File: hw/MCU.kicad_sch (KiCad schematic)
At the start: 19 parts, among them J2 Conn_01x06, J7 Conn_01x04, SW2 SKRPACE010, SW3 SKRPACE010, U2 N32L406RBL7, Y2 XL2EL89COI-111YLC-8M

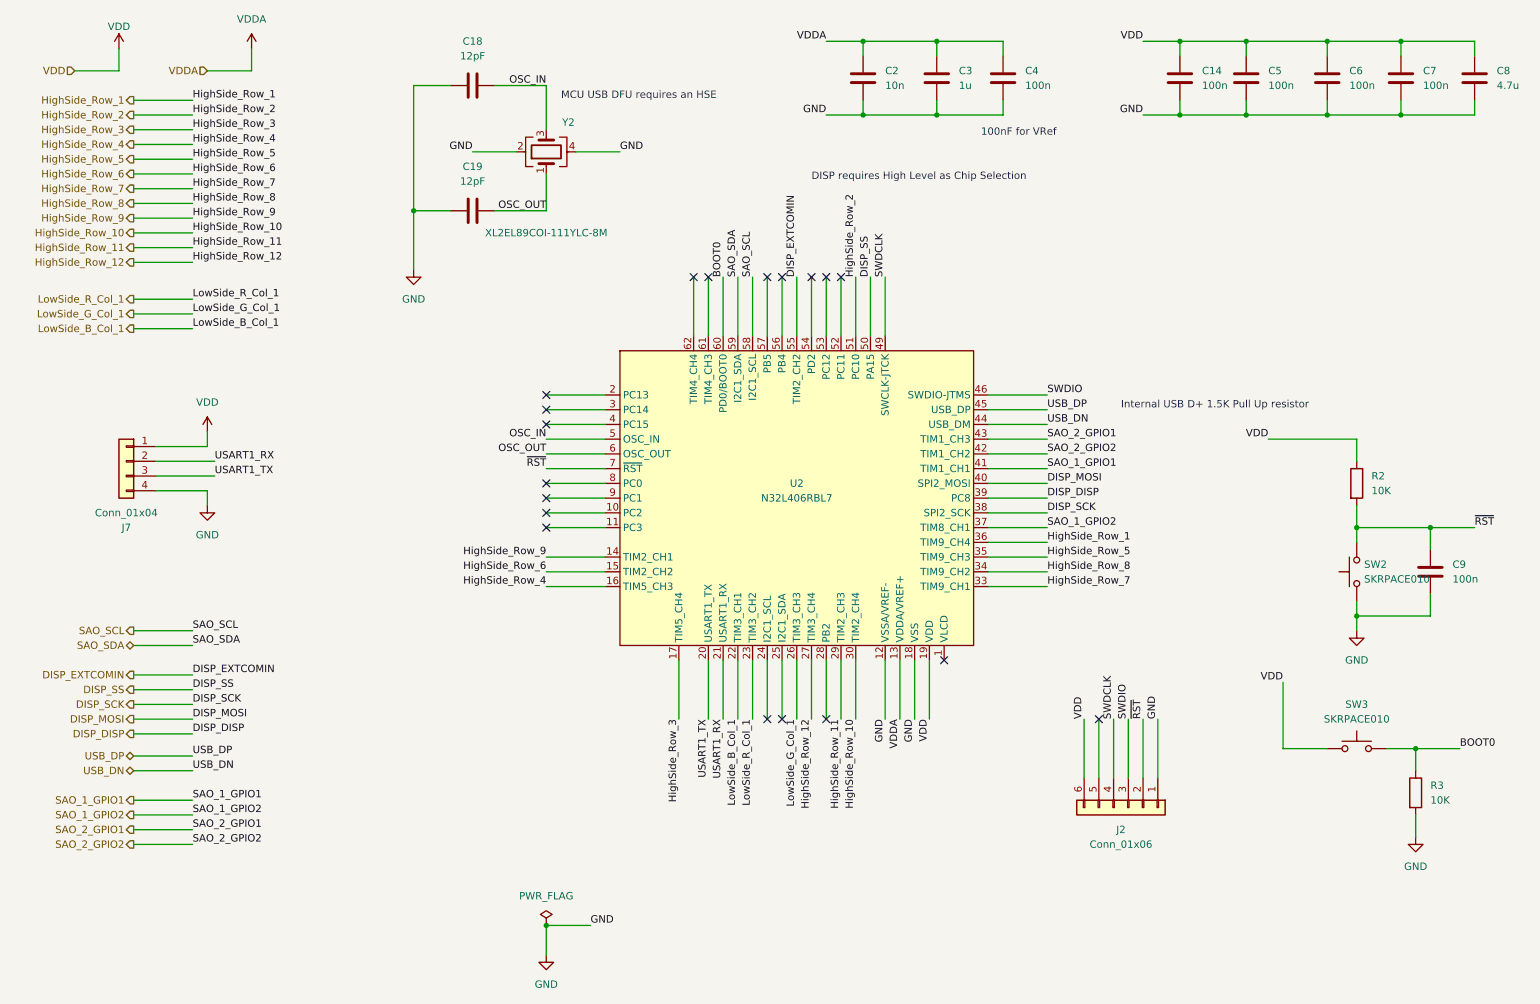
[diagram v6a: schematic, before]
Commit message: changed some pin connections
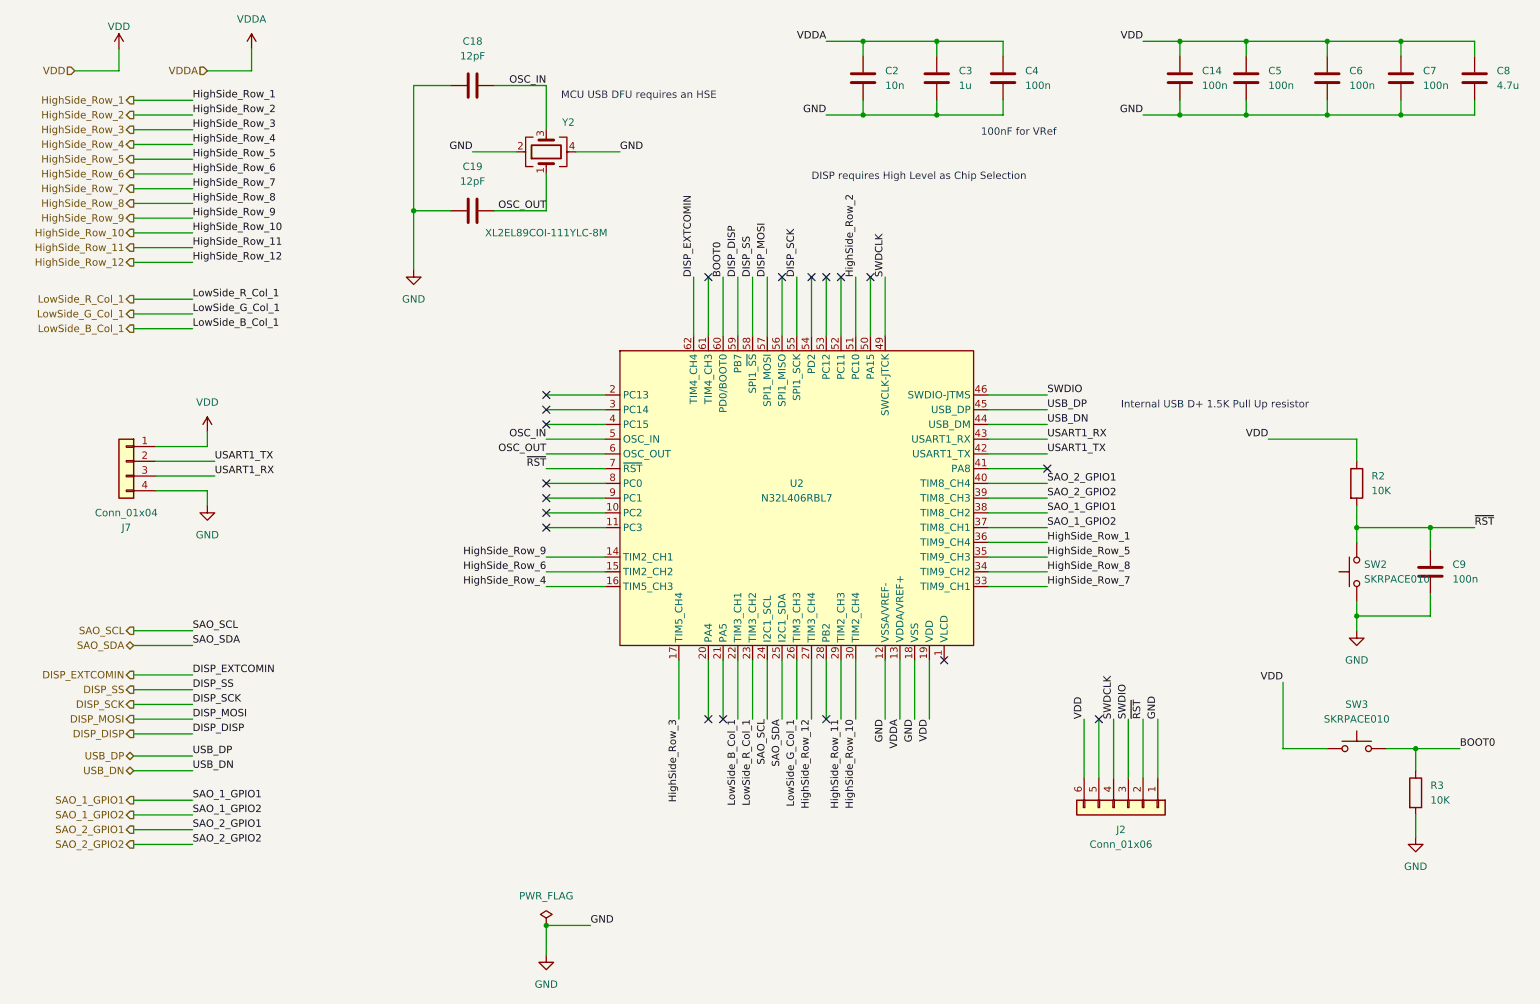
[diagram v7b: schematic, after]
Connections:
- net DISP_DISP: now also U2.59 (PB7); no longer U2.39 (PC8)
- net DISP_EXTCOMIN: now also U2.62 (PB9); no longer U2.55 (PB3)
- net DISP_MOSI: now also U2.57 (PB5); no longer U2.40 (PC9)
- net DISP_SCK: now also U2.55 (PB3); no longer U2.38 (PC7)
- net DISP_SS: now also U2.58 (PB6); no longer U2.50 (PA15)
- net SAO_1_GPIO1: now also U2.38 (PC7); no longer U2.41 (PA8)
- net SAO_2_GPIO1: now also U2.40 (PC9); no longer U2.43 (PA10)
- net SAO_2_GPIO2: now also U2.39 (PC8); no longer U2.42 (PA9)
- net SAO_SCL: now also U2.24 (PC4); no longer U2.58 (PB6)
- net SAO_SDA: now also U2.25 (PC5); no longer U2.59 (PB7)
- net USART1_RX: now also J7.3 (Pin_3), U2.43 (PA10); no longer J7.2 (Pin_2), U2.21 (PA5)
- net USART1_TX: now also J7.2 (Pin_2), U2.42 (PA9); no longer J7.3 (Pin_3), U2.20 (PA4)
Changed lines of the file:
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@@
   (no_connect (at 182.88 127))
   (no_connect (at 162.56 60.96))
-  (no_connect (at 154.94 137.16))
-  (no_connect (at 152.4 137.16))
   (no_connect (at 142.24 60.96))
+  (no_connect (at 170.18 60.96))
+  (no_connect (at 142.24 137.16))
+  (no_connect (at 200.66 93.98))
   (no_connect (at 114.3 86.36))
-  (no_connect (at 139.7 60.96))
+  (no_connect (at 154.94 60.96))
   (no_connect (at 114.3 99.06))
   (no_connect (at 209.55 137.16))
   (no_connect (at 114.3 96.52))
   (no_connect (at 165.1 60.96))
-  (no_connect (at 152.4 60.96))
   (no_connect (at 160.02 60.96))
   (no_connect (at 114.3 81.28))
-  (no_connect (at 154.94 60.96))
+  (no_connect (at 144.78 137.16))
   (no_connect (at 114.3 104.14))
   (no_connect (at 114.3 83.82))
@@
     (effects (font (size 1.27 1.27)) (justify right bottom))
   )
-  (label "DISP_EXTCOMIN" (at 157.48 60.96 90) (fields_autoplaced)
+  (label "DISP_EXTCOMIN" (at 139.7 60.96 90) (fields_autoplaced)
     (effects (font (size 1.27 1.27)) (justify left bottom))
   )
@@
     (effects (font (size 1.27 1.27)) (justify left bottom))
   )
-  (label "SAO_SDA" (at 147.32 60.96 90) (fields_autoplaced)
-    (effects (font (size 1.27 1.27)) (justify left bottom))
+  (label "SAO_SDA" (at 154.94 137.16 270) (fields_autoplaced)
+    (effects (font (size 1.27 1.27)) (justify right bottom))
   )
   (label "~{RST}" (at 114.3 93.98 180) (fields_autoplaced)
@@
     (effects (font (size 1.27 1.27)) (justify left bottom))
   )
-  (label "USART1_TX" (at 57.15 95.25 0) (fields_autoplaced)
+  (label "USART1_TX" (at 57.15 92.71 0) (fields_autoplaced)
     (effects (font (size 1.27 1.27)) (justify left bottom))
   )
@@
     (effects (font (size 1.27 1.27)) (justify right bottom))
   )
-  (label "SAO_2_GPIO2" (at 200.66 91.44 0) (fields_autoplaced)
+  (label "SAO_2_GPIO2" (at 200.66 99.06 0) (fields_autoplaced)
     (effects (font (size 1.27 1.27)) (justify left bottom))
   )
@@
     (effects (font (size 1.27 1.27)) (justify right bottom))
   )
-  (label "USART1_RX" (at 144.78 137.16 270) (fields_autoplaced)
-    (effects (font (size 1.27 1.27)) (justify right bottom))
-  )
   (label "OSC_IN" (at 114.3 27.94 180) (fields_autoplaced)
     (effects (font (size 1.27 1.27)) (justify right bottom))
@@
     (effects (font (size 1.27 1.27)) (justify left bottom))
   )
-  (label "SAO_SCL" (at 149.86 60.96 90) (fields_autoplaced)
-    (effects (font (size 1.27 1.27)) (justify left bottom))
+  (label "SAO_SCL" (at 152.4 137.16 270) (fields_autoplaced)
+    (effects (font (size 1.27 1.27)) (justify right bottom))
   )
-  (label "SAO_2_GPIO1" (at 200.66 88.9 0) (fields_autoplaced)
+  (label "SAO_2_GPIO1" (at 200.66 96.52 0) (fields_autoplaced)
     (effects (font (size 1.27 1.27)) (justify left bottom))
   )
@@
     (effects (font (size 1.27 1.27)) (justify left bottom))
   )
-  (label "DISP_SCK" (at 200.66 101.6 0) (fields_autoplaced)
+  (label "DISP_SCK" (at 157.48 60.96 90) (fields_autoplaced)
     (effects (font (size 1.27 1.27)) (justify left bottom))
   )
@@
     (effects (font (size 1.27 1.27)) (justify left bottom))
   )
-  (label "DISP_MOSI" (at 200.66 96.52 0) (fields_autoplaced)
+  (label "DISP_MOSI" (at 152.4 60.96 90) (fields_autoplaced)
     (effects (font (size 1.27 1.27)) (justify left bottom))
   )
@@
     (effects (font (size 1.27 1.27)) (justify left bottom))
   )
+  (label "USART1_RX" (at 200.66 88.9 0) (fields_autoplaced)
+    (effects (font (size 1.27 1.27)) (justify left bottom))
+  )
   (label "DISP_MOSI" (at 53.34 137.16 0) (fields_autoplaced)
     (effects (font (size 1.27 1.27)) (justify left bottom))
@@
     (effects (font (size 1.27 1.27)) (justify right bottom))
   )
-  (label "USART1_TX" (at 142.24 137.16 270) (fields_autoplaced)
-    (effects (font (size 1.27 1.27)) (justify right bottom))
-  )
   (label "LowSide_R_Col_1" (at 53.34 64.77 0) (fields_autoplaced)
     (effects (font (size 1.27 1.27)) (justify left bottom))
@@
     (effects (font (size 1.27 1.27)) (justify left bottom))
   )
-  (label "DISP_SS" (at 170.18 60.96 90) (fields_autoplaced)
+  (label "DISP_SS" (at 149.86 60.96 90) (fields_autoplaced)
     (effects (font (size 1.27 1.27)) (justify left bottom))
   )
@@
     (effects (font (size 1.27 1.27)) (justify right bottom))
   )
+  (label "USART1_TX" (at 200.66 91.44 0) (fields_autoplaced)
+    (effects (font (size 1.27 1.27)) (justify left bottom))
+  )
   (label "DISP_DISP" (at 53.34 139.7 0) (fields_autoplaced)
     (effects (font (size 1.27 1.27)) (justify left bottom))
@@
     (effects (font (size 1.27 1.27)) (justify left bottom))
   )
-  (label "SAO_1_GPIO1" (at 200.66 93.98 0) (fields_autoplaced)
+  (label "SAO_1_GPIO1" (at 200.66 101.6 0) (fields_autoplaced)
     (effects (font (size 1.27 1.27)) (justify left bottom))
   )
@@
     (effects (font (size 1.27 1.27)) (justify left bottom))
   )
-  (label "DISP_DISP" (at 200.66 99.06 0) (fields_autoplaced)
+  (label "DISP_DISP" (at 147.32 60.96 90) (fields_autoplaced)
     (effects (font (size 1.27 1.27)) (justify left bottom))
   )
-  (label "USART1_RX" (at 57.15 92.71 0) (fields_autoplaced)
+  (label "USART1_RX" (at 57.15 95.25 0) (fields_autoplaced)
     (effects (font (size 1.27 1.27)) (justify left bottom))
   )
@@
     (pin "19")
     (pin "2")
-    (pin "20" (alternate "USART1_TX"))
-    (pin "21" (alternate "USART1_RX"))
+    (pin "20")
+    (pin "21")
     (pin "22" (alternate "TIM3_CH1"))
     (pin "23" (alternate "TIM3_CH2"))
@@
     (pin "36" (alternate "TIM9_CH4"))
     (pin "37" (alternate "TIM8_CH1"))
-    (pin "38" (alternate "SPI2_SCK"))
-    (pin "39")
+    (pin "38" (alternate "TIM8_CH2"))
+    (pin "39" (alternate "TIM8_CH3"))
     (pin "4")
-    (pin "40" (alternate "SPI2_MOSI"))
-    (pin "41" (alternate "TIM1_CH1"))
-    (pin "42" (alternate "TIM1_CH2"))
-    (pin "43" (alternate "TIM1_CH3"))
+    (pin "40" (alternate "TIM8_CH4"))
+    (pin "41")
+    (pin "42" (alternate "USART1_TX"))
+    (pin "43" (alternate "USART1_RX"))
     (pin "44" (alternate "USB_DM"))
     (pin "45" (alternate "USB_DP"))
@@
     (pin "53")
     (pin "54")
-    (pin "55" (alternate "TIM2_CH2"))
-    (pin "56")
-    (pin "57")
-    (pin "58" (alternate "I2C1_SCL"))
-    (pin "59" (alternate "I2C1_SDA"))
+    (pin "55" (alternate "SPI1_SCK"))
+    (pin "56" (alternate "SPI1_MISO"))
+    (pin "57" (alternate "SPI1_MOSI"))
+    (pin "58" (alternate "SPI1_~{SS}"))
+    (pin "59")
     (pin "6" (alternate "OSC_OUT"))
     (pin "60")
